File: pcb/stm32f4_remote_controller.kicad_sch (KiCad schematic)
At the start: 30 parts, among them J1 Conn_01x04_Pin, SW1 SW_Push, SW2 SW_DPDT_x2, U1 STM32F401CCU6, U2 OLED DISPLAY, U6 TPS61021ADSGR, Y1 8Mhz

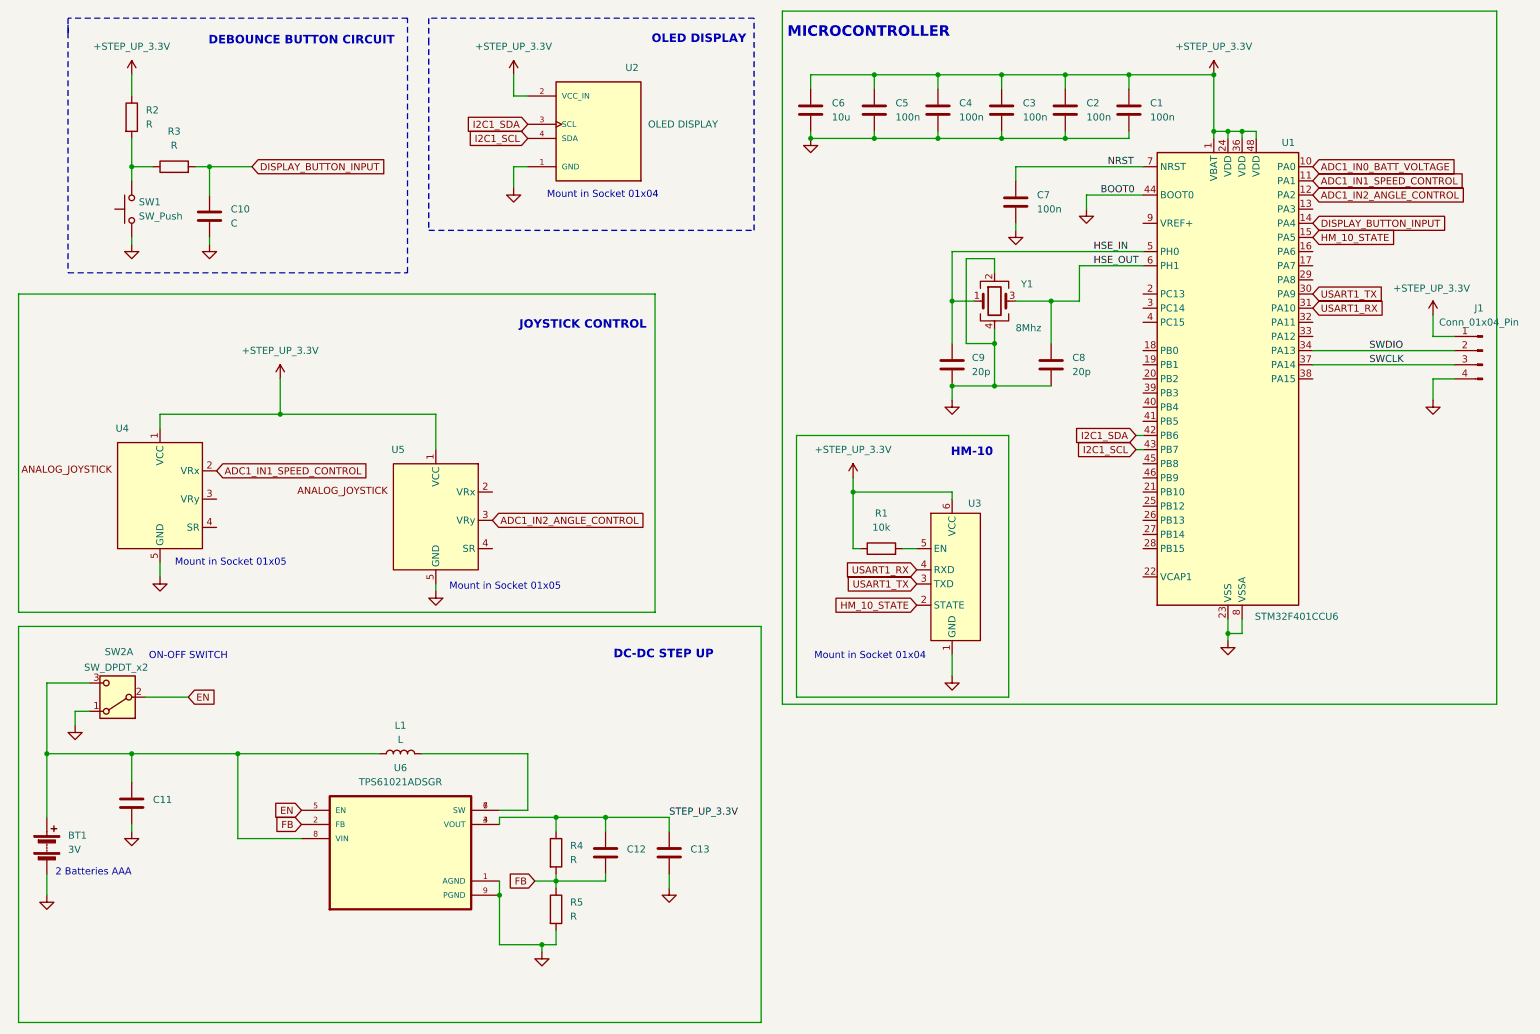
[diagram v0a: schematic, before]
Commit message: pcb: add values to component on sch
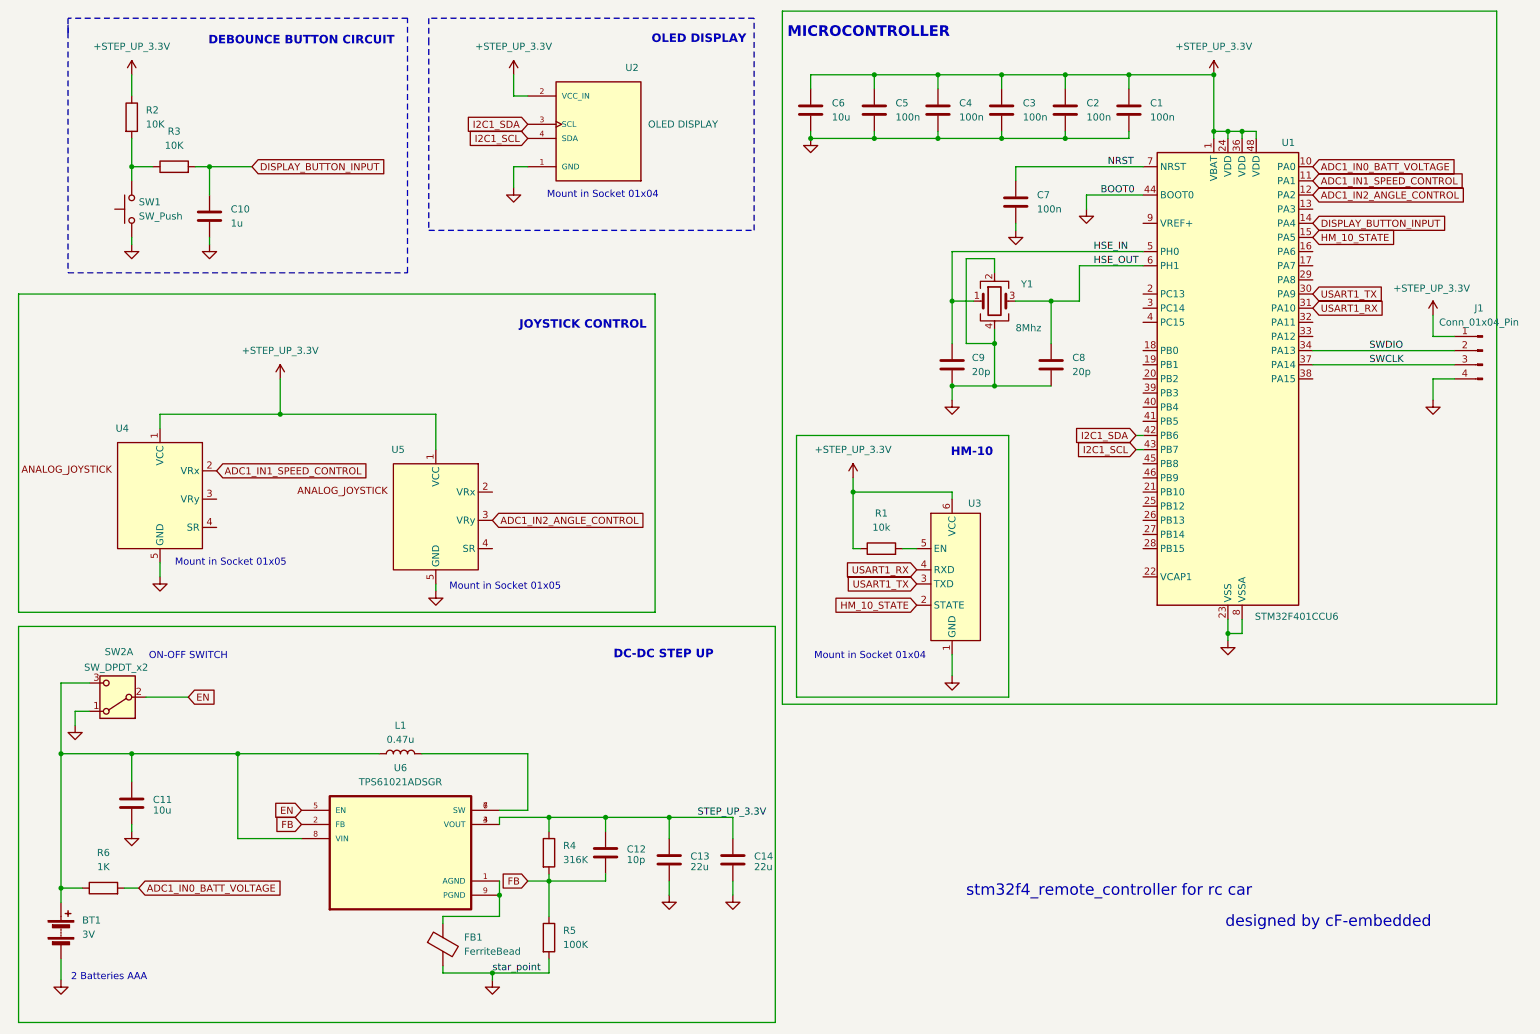
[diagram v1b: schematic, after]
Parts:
- added C14: 22u, symbol Device:C
- added FB1: FerriteBead, symbol Device:FerriteBead
- added R6: 1K, symbol Device:R
- C10: value C -> 1u
- C11: value ~ -> 10u
- C12: value ~ -> 10p
- C13: value ~ -> 22u
- L1: value L -> 0.47u
- R2, R3: value R -> 10K
- R4: value R -> 316K
- R5: value R -> 100K
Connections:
- net ADC1_IN0_BATT_VOLTAGE: now also R6.2
- net GND: now also C14.2, FB1.2; no longer U6.1 (AGND), U6.9 (PGND)
- net STEP_UP_3.3V: now also C14.1
- net at BT1.1 (+), C11.1, L1.1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: now also R6.1
- new net: FB1.1, U6.1 (AGND), U6.9 (PGND)
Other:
- note added: "designed by cF-embedded"
- note added: "stm32f4_remote_controller for rc car"
- moved on the sheet: BT1, C13, R4, R5

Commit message: pcb: add reset button on sch
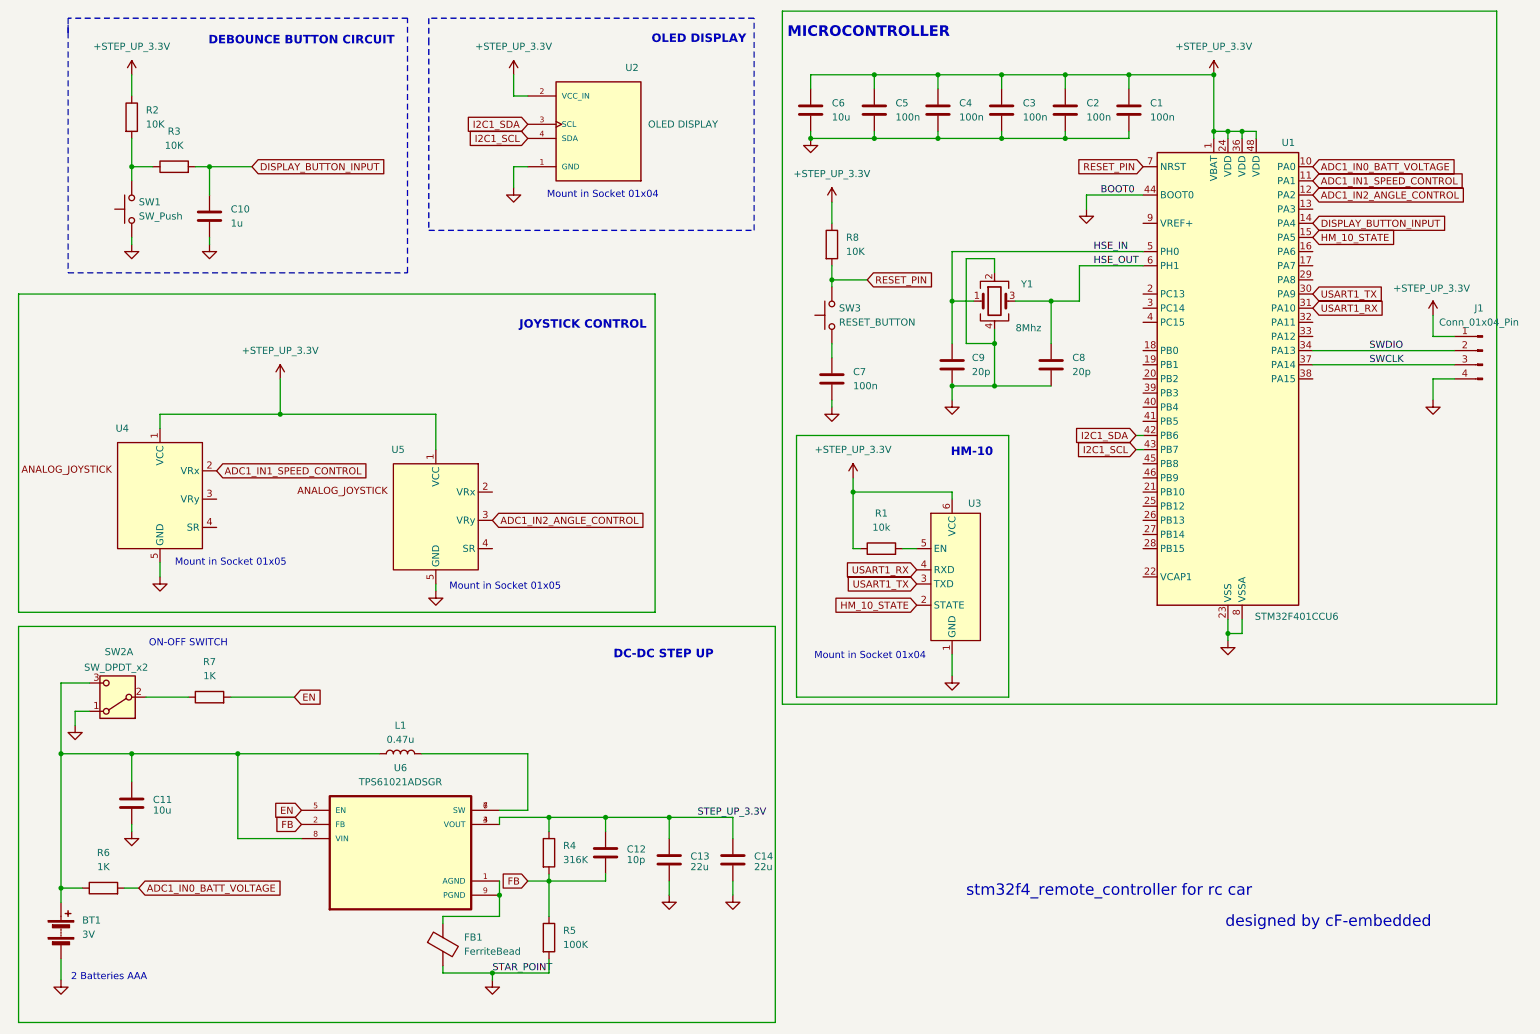
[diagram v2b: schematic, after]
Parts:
- added R7: 1K, symbol Device:R
- added R8: 10K, symbol Device:R
- added SW3: RESET_BUTTON, symbol Switch:SW_Push
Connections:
- net +STEP_UP_3.3V: now also R8.1
- net EN: now also R7.2; no longer SW2.2 (B)
- net NRST: no longer names the net of C7.1
- net NRST: now also SW3.1; no longer U1.7 (NRST)
- new net: R7.1, SW2.2 (B)
- new net RESET_PIN: R8.2, SW3.2, U1.7 (NRST)
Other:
- moved on the sheet: C7

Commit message: pcb: connect vcap to gnd
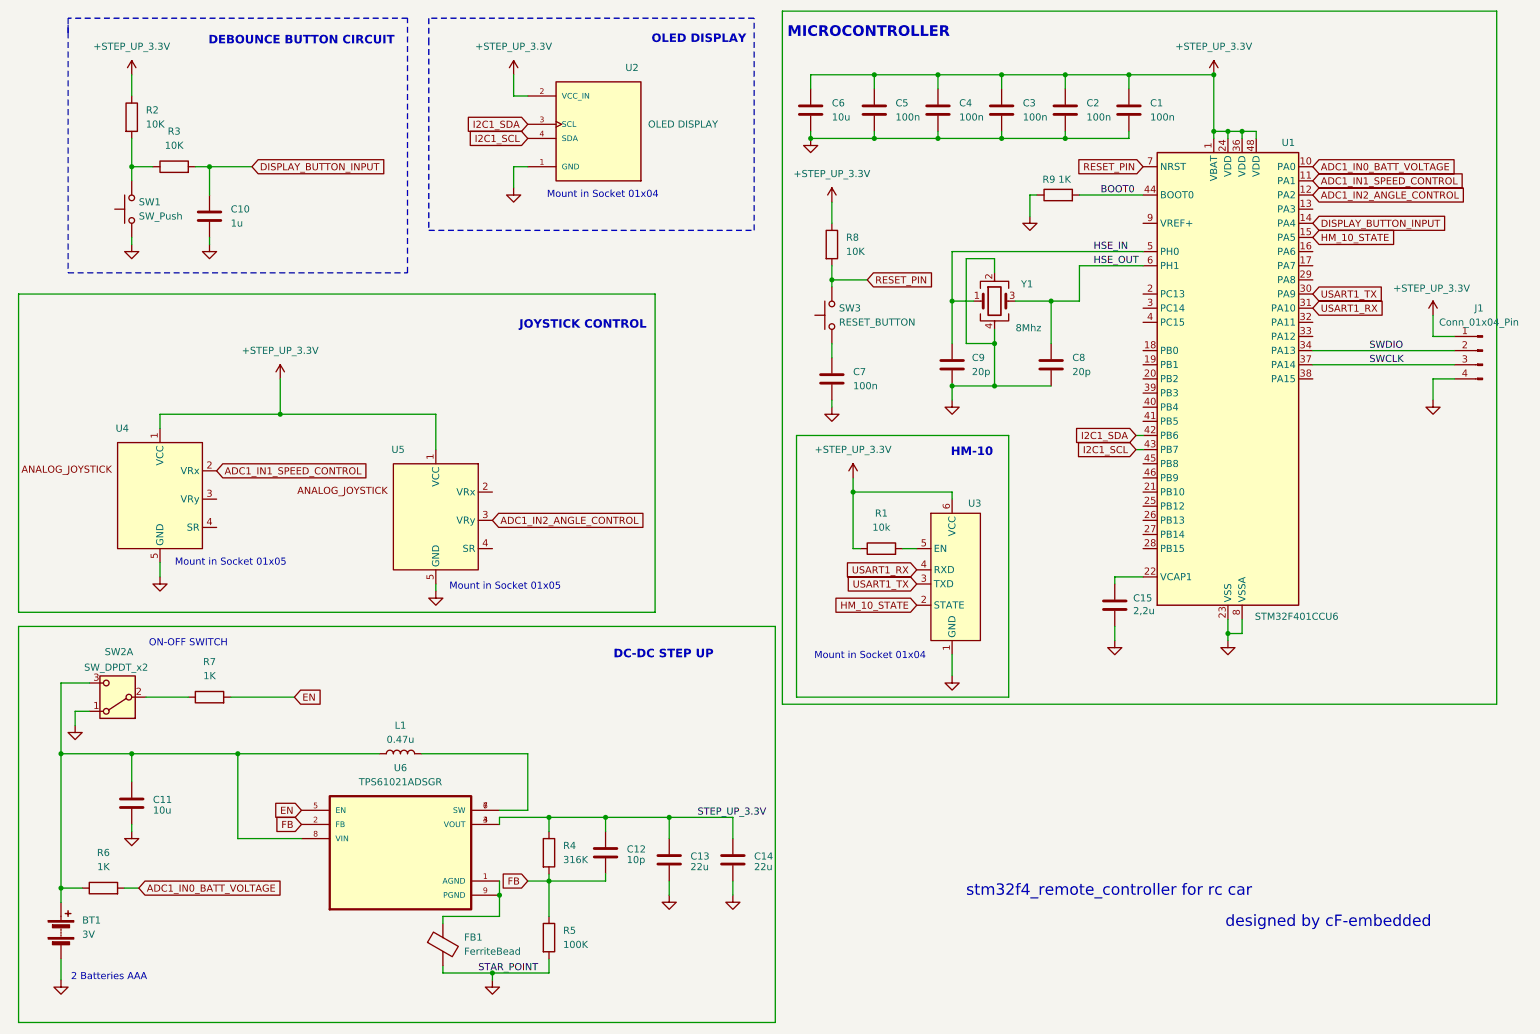
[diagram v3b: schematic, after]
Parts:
- added C15: 2,2u, symbol Device:C
- added R9: 1K, symbol Device:R
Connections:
- net GND: now also C15.2, R9.1; no longer U1.44 (BOOT0)
- net at U1.22 (VCAP1): now also C15.1
- new net BOOT0: R9.2, U1.44 (BOOT0)

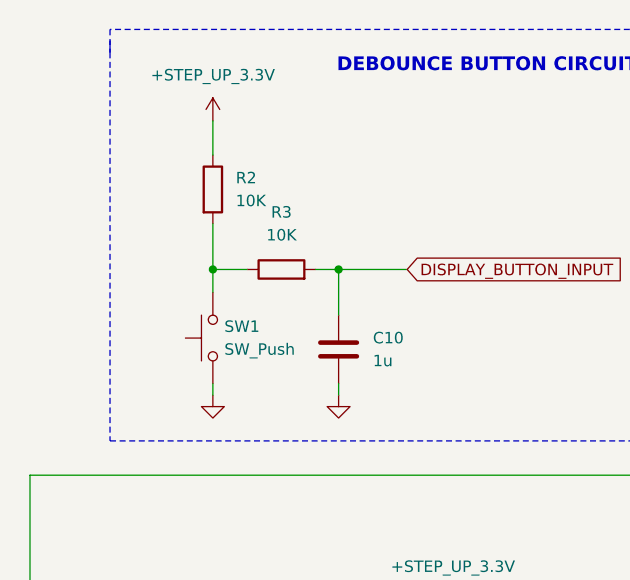
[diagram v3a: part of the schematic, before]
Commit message: pcb: add footprints to elements
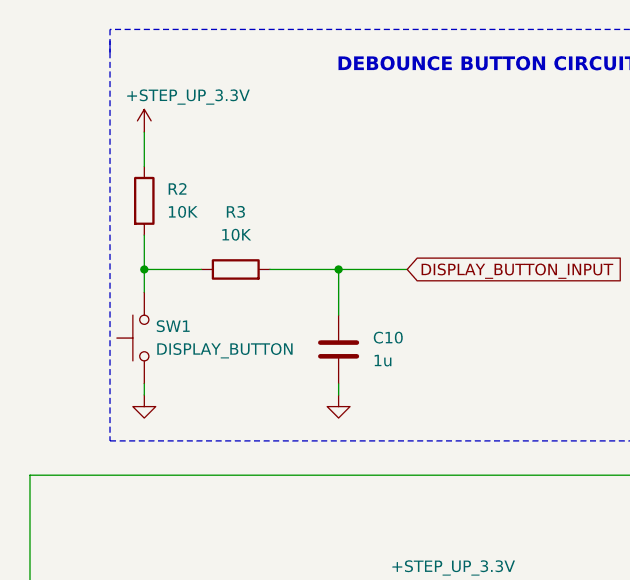
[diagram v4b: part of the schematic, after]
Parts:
- BT1: footprint (none) -> Battery:BatteryHolder_Keystone_2468_2xAAA
- C1, C2, C3, C4, C5, C7: footprint (none) -> Capacitor_SMD:C_0402_1005Metric
- C10, C11, C15, C6: footprint (none) -> Capacitor_SMD:C_0603_1608Metric
- C12, C8, C9: footprint (none) -> Capacitor_SMD:C_0201_0603Metric
- C13, C14: footprint (none) -> Capacitor_SMD:C_0805_2012Metric
- FB1: footprint (none) -> Inductor_SMD:L_0603_1608Metric
- J1: footprint (none) -> Connector_PinHeader_2.54mm:PinHeader_1x04_P2.54mm_Vertical
- L1: footprint (none) -> Inductor_SMD:L_7.3x7.3_H4.5
- R1, R2, R3, R6, R7, R8, R9: footprint (none) -> Resistor_SMD:R_0402_1005Metric
- R4, R5: footprint (none) -> Resistor_SMD:R_0805_2012Metric
- SW1: value SW_Push -> DISPLAY_BUTTON; footprint (none) -> Button_Switch_THT:Push_E-Switch_KS01Q01
- SW2: footprint (none) -> Button_Switch_THT:SW_CK_JS202011AQN_DPDT_Angled
- SW3: footprint (none) -> Button_Switch_THT:SW_PUSH-12mm
- U3: footprint (none) -> Connector_Molex:Molex_SL_171971-0006_1x06_P2.54mm_Vertical
- U4, U5: footprint (none) -> Connector_Molex:Molex_SL_171971-0005_1x05_P2.54mm_Vertical
- Y1: footprint (none) -> Crystal:Crystal_SMD_5032-4Pin_5.0x3.2mm
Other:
- moved on the sheet: R2, R3, SW1

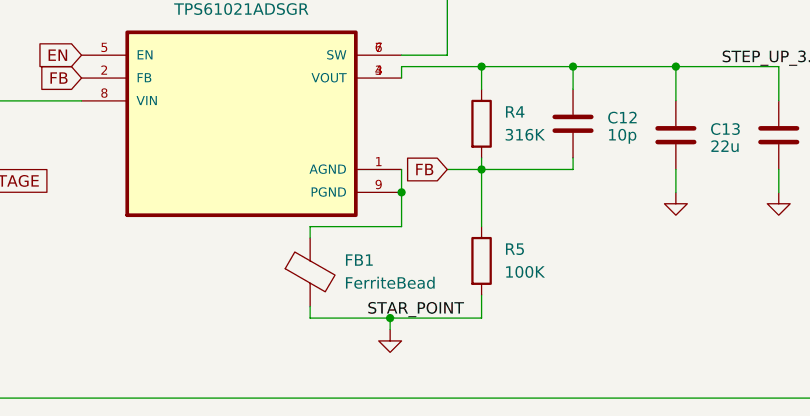
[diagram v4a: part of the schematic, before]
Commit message: pcb: add first version of pcb
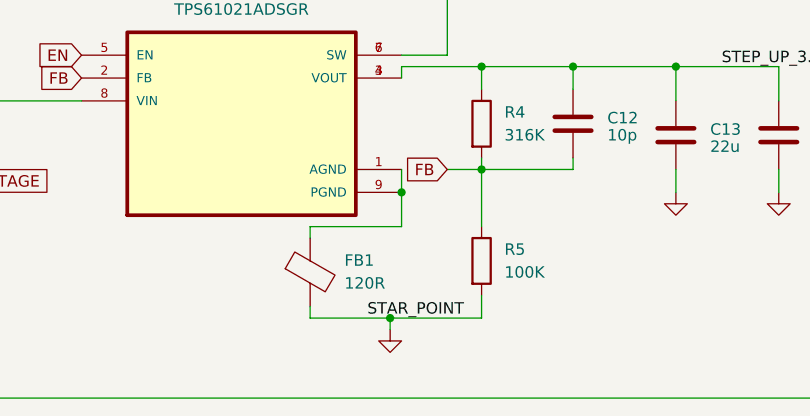
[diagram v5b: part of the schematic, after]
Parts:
- FB1: value FerriteBead -> 120R
- L1: footprint Inductor_SMD:L_7.3x7.3_H4.5 -> Inductor_SMD:L_01005_0402Metric
- U2: footprint DM-OLED096-636:MODULE_DM-OLED096-636 -> OLED-DISPLAY-128x64:MODULE_DM-OLED096-636
- U6: footprint TPS61021ADSGR:SON50P200X200X80-9N -> dc-dc_step-up:SON50P200X200X80-9N
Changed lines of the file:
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@@
 			)
 		)
-		(property "Value" "FerriteBead"
+		(property "Value" "120R"
 			(at 95.25 182.8291 0)
 			(effects
@@
 			)
 		)
-		(property "Footprint" "DM-OLED096-636:MODULE_DM-OLED096-636"
+		(property "Footprint" "OLED-DISPLAY-128x64:MODULE_DM-OLED096-636"
 			(at 119.38 36.83 0)
 			(effects
@@
 			)
 		)
-		(property "Footprint" "Inductor_SMD:L_7.3x7.3_H4.5"
+		(property "Footprint" "Inductor_SMD:L_01005_0402Metric"
 			(at 83.82 147.32 0)
 			(effects
@@
 			)
 		)
-		(property "Footprint" "TPS61021ADSGR:SON50P200X200X80-9N"
+		(property "Footprint" "dc-dc_step-up:SON50P200X200X80-9N"
 			(at 83.82 165.1 0)
 			(effects

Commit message: pcb: add ready pcb
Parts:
- added H1, H2, H3, H4: MountingHole, MountingHole:MountingHole_2.5mm, symbol Mechanical:MountingHole
- BT1: footprint Battery:BatteryHolder_Keystone_2468_2xAAA -> Connector_Phoenix_GMSTB:PhoenixContact_GMSTBA_2,5_2-G-7,62_1x02_P7.62mm_Horizontal
- C12, C8, C9: footprint Capacitor_SMD:C_0201_0603Metric -> Capacitor_SMD:C_0402_1005Metric
- L1: footprint Inductor_SMD:L_01005_0402Metric -> Inductor_SMD:L_1206_3216Metric
- SW1: footprint Button_Switch_THT:Push_E-Switch_KS01Q01 -> Connector_PinHeader_2.54mm:PinHeader_1x02_P2.54mm_Vertical
- SW3: footprint Button_Switch_THT:SW_PUSH-12mm -> Button_Switch_THT:SW_PUSH_6mm
- U2: footprint OLED-DISPLAY-128x64:MODULE_DM-OLED096-636 -> Connector_PinHeader_2.54mm:PinHeader_1x04_P2.54mm_Vertical
- U4, U5: footprint Connector_Molex:Molex_SL_171971-0005_1x05_P2.54mm_Vertical -> Connector_PinHeader_2.54mm:PinHeader_1x05_P2.54mm_Vertical
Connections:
- net STEP_UP_3.3V is gone; now on net +STEP_UP_3.3V: C12.1, C13.1, C14.1, R4.1, U6.3 (VOUT), U6.4 (VOUT)
- net DISPLAY_BUTTON_INPUT: now also U1.41 (PB5); no longer U1.14 (PA4)
- net GND: now also U3.2 (STATE)
- net USART2_RX: now reaches U1.13 (PA3)
- net USART2_RX: now also U3.4 (RXD)
- net ADC1_IN0_BATT_VOLTAGE renamed ADC1_IN0_SPEED_CONTROL
- net ADC1_IN0_SPEED_CONTROL: now also U4.2 (VRx); no longer R6.2
- net ADC1_IN1_SPEED_CONTROL renamed ADC1_IN1_ANGLE_CONTROL
- net ADC1_IN1_ANGLE_CONTROL: now also U5.3 (VRy); no longer U4.2 (VRx)
- net ADC1_IN2_ANGLE_CONTROL renamed USART2_TX
- net USART2_TX: now also U3.3 (TXD); no longer U5.3 (VRy)
- net HM_10_STATE: no longer names the net of U1.15 (PA5)
- net HM_10_STATE: no longer U3.2 (STATE)
- net USART1_RX: no longer names the net of U1.31 (PA10)
- net USART1_RX: no longer U3.4 (RXD)
- net USART1_TX: no longer names the net of U1.30 (PA9)
- net USART1_TX: no longer U3.3 (TXD)
- new net ADC1_IN4_BATT_VOLTAGE: R6.2, U1.14 (PA4)
- no-connect marks 0 -> 29
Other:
- note added: "MOUNTING HOLES"
